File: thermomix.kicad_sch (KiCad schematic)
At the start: 30 parts, among them J101 DX07S016JA1R1500, J102 Conn_01x05, SW101 SW_Push, SW102 SW_Push, U101 MIC5353-3.3YMT, U102 TPD2E2U06, U103 STM32F303RDTx, Y101 Crystal_GND24

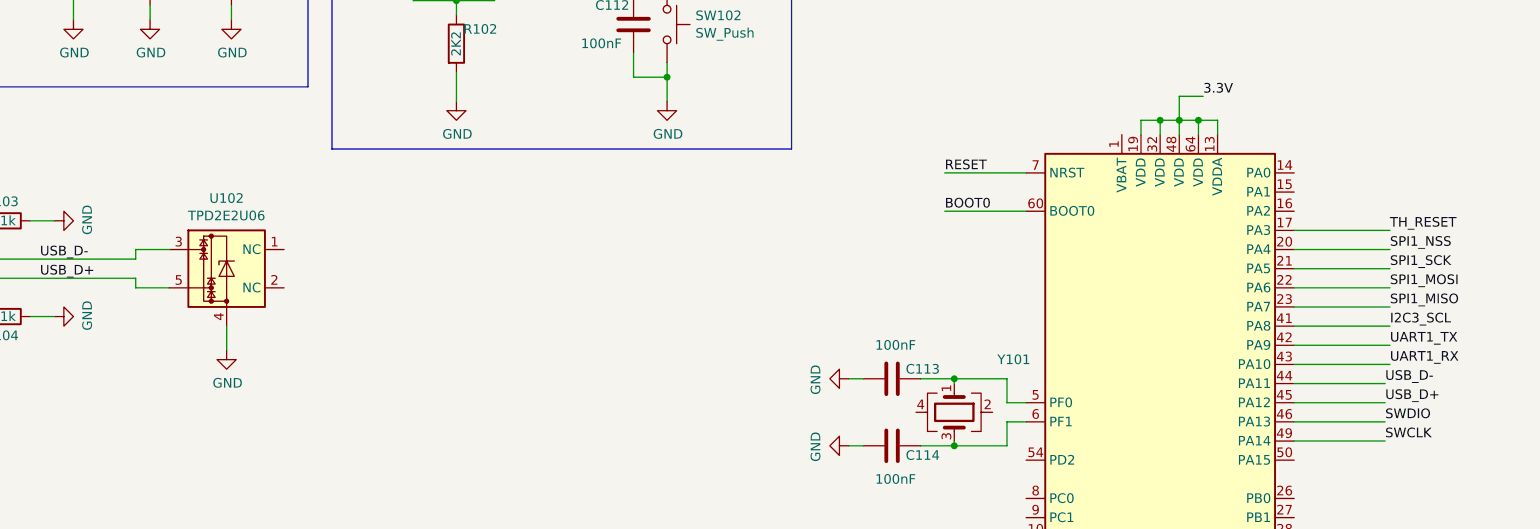
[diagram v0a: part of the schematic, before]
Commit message: Fixes issues from revision 1.0
Signed-off-by: Alexis Jeandet <alexis.jeandet@member.fsf.org>
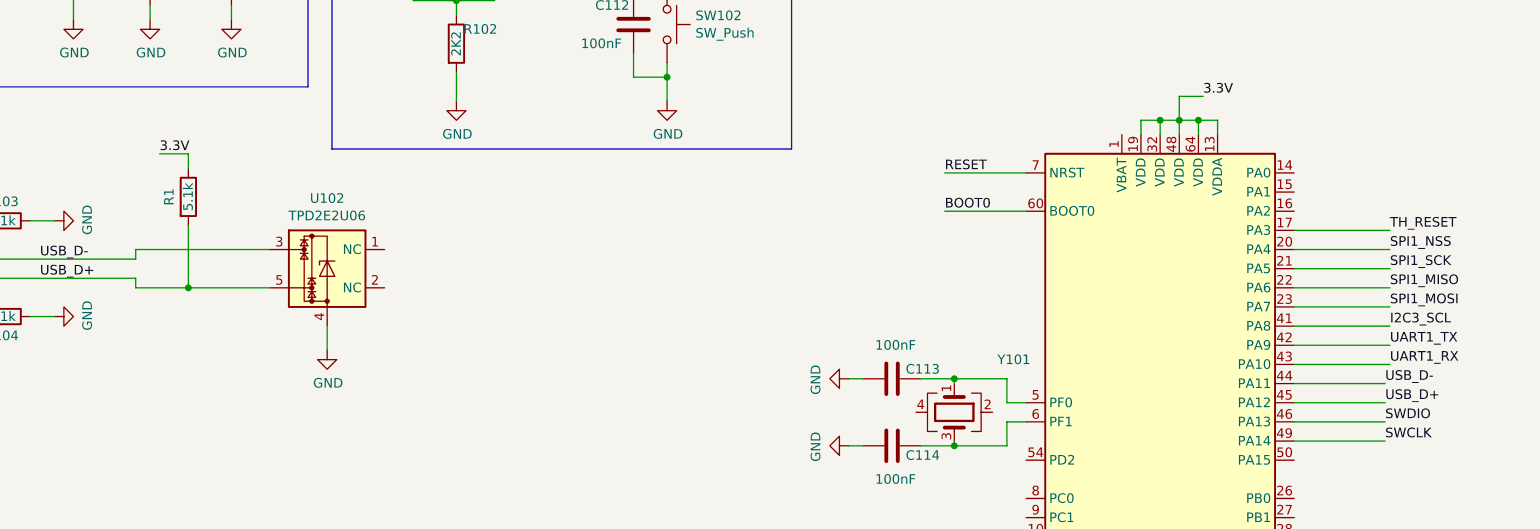
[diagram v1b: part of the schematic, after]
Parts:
- added R1: 5.1k, Resistor_SMD:R_0603_1608Metric_Pad0.98x0.95mm_HandSolder, symbol Device:R
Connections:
- net 3.3V: now also R1.1
- net SPI1_MISO: now also U103.22 (PA6); no longer U103.23 (PA7)
- net SPI1_MOSI: now also U103.23 (PA7); no longer U103.22 (PA6)
- net USB_D+: now also R1.2
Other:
- company: (none) -> LPP/CNRS
- moved on the sheet: U102
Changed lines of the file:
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@@
 (kicad_sch (version 20211123) (generator eeschema)
   (paper "A4")
+  (title_block
+    (date "2023-02-07")
+    (rev "1.1")
+    (company "LPP/CNRS")
+  )
   (junction (at 132.715 29.845) (diameter 0) (color 0 0 0 0)
   )
@@
   )
   (junction (at 198.755 91.44) (diameter 0) (color 0 0 0 0)
+  )
+  (junction (at 97.155 79.375) (diameter 0) (color 0 0 0 0)
   )
   (no_connect (at 65.405 73.025))
@@
     (stroke (width 0) (type default) (color 0 0 0 0))
   )
-  (wire (pts (xy 102.235 84.455) (xy 102.235 87.63))
+  (wire (pts (xy 93.345 61.595) (xy 97.155 61.595))
+    (stroke (width 0) (type default) (color 0 0 0 0))
+  )
+  (wire (pts (xy 115.57 84.455) (xy 115.57 87.63))
     (stroke (width 0) (type default) (color 0 0 0 0))
   )
@@
     (stroke (width 0) (type default) (color 0 0 0 0))
   )
+  (wire (pts (xy 97.155 61.595) (xy 97.155 63.5))
+    (stroke (width 0) (type default) (color 0 0 0 0))
+  )
   (wire (pts (xy 223.52 57.15) (xy 226.06 57.15))
     (stroke (width 0) (type default) (color 0 0 0 0))
@@
     (stroke (width 0) (type default) (color 0 0 0 0))
   )
-  (wire (pts (xy 94.615 79.375) (xy 90.17 79.375))
+  (wire (pts (xy 107.95 79.375) (xy 97.155 79.375))
     (stroke (width 0) (type default) (color 0 0 0 0))
   )
@@
     (stroke (width 0) (type default) (color 0 0 0 0))
   )
+  (wire (pts (xy 97.155 71.12) (xy 97.155 79.375))
+    (stroke (width 0) (type default) (color 0 0 0 0))
+  )
   (wire (pts (xy 233.68 57.15) (xy 233.68 59.055))
     (stroke (width 0) (type default) (color 0 0 0 0))
@@
     (stroke (width 0) (type default) (color 0 0 0 0))
   )
+  (wire (pts (xy 97.155 79.375) (xy 90.17 79.375))
+    (stroke (width 0) (type default) (color 0 0 0 0))
+  )
   (wire (pts (xy 102.87 43.815) (xy 102.87 41.91))
     (stroke (width 0) (type default) (color 0 0 0 0))
@@
     (stroke (width 0) (type default) (color 0 0 0 0))
   )
-  (wire (pts (xy 94.615 74.295) (xy 90.17 74.295))
+  (wire (pts (xy 107.95 74.295) (xy 90.17 74.295))
     (stroke (width 0) (type default) (color 0 0 0 0))
   )
@@
     (effects (font (size 1.27 1.27)) (justify left bottom))
   )
-  (label "SPI1_MISO" (at 256.54 81.915 0)
+  (label "SPI1_MISO" (at 256.54 79.375 0)
     (effects (font (size 1.27 1.27)) (justify left bottom))
   )
@@
     (effects (font (size 1.27 1.27)) (justify left bottom))
   )
-  (label "SPI1_MOSI" (at 256.54 79.375 0)
+  (label "SPI1_MOSI" (at 256.54 81.915 0)
     (effects (font (size 1.27 1.27)) (justify left bottom))
   )
@@
   )
   (label "RESET" (at 124.46 183.515 0)
+    (effects (font (size 1.27 1.27)) (justify left bottom))
+  )
+  (label "3.3V" (at 93.345 61.595 0)
     (effects (font (size 1.27 1.27)) (justify left bottom))
   )
@@
     )
     (pin "1")
+  )
+  (symbol (lib_id "Device:R") (at 97.155 67.31 0) (unit 1)
+    (in_bom yes) (on_board yes)
+    (property "Reference" "R1" (id 0) (at 94.615 67.31 90))
+    (property "Value" "5.1k" (id 1) (at 97.155 67.31 90))
+    (property "Footprint" "Resistor_SMD:R_0603_1608Metric_Pad0.98x0.95mm_HandSolder" (id 2) (at 95.377 67.31 90)
+      (effects (font (size 1.27 1.27)) hide)
+    )
+    (property "Datasheet" "~" (id 3) (at 97.155 67.31 0)
+      (effects (font (size 1.27 1.27)) hide)
+    )
+    (pin "1")
+    (pin "2")
   )
   (symbol (lib_id "power:GND") (at 240.03 33.02 0) (unit 1)
@@
     (pin "S6")
   )
-  (symbol (lib_id "Power_Protection:TPD2E2U06") (at 102.235 76.835 0) (unit 1)
-    (in_bom yes) (on_board yes)
-    (property "Reference" "U102" (id 0) (at 102.235 67.5132 0))
-    (property "Value" "TPD2E2U06" (id 1) (at 102.235 69.8246 0))
-    (property "Footprint" "Package_TO_SOT_SMD:SOT-553" (id 2) (at 81.915 83.185 0)
-      (effects (font (size 1.27 1.27)) hide)
-    )
-    (property "Datasheet" "http://www.ti.com/lit/ds/symlink/tpd2e2u06.pdf" (id 3) (at 97.155 71.755 0)
+  (symbol (lib_id "Power_Protection:TPD2E2U06") (at 115.57 76.835 0) (unit 1)
+    (in_bom yes) (on_board yes)
+    (property "Reference" "U102" (id 0) (at 115.57 67.5132 0))
+    (property "Value" "TPD2E2U06" (id 1) (at 115.57 69.8246 0))
+    (property "Footprint" "Package_TO_SOT_SMD:SOT-553" (id 2) (at 95.25 83.185 0)
+      (effects (font (size 1.27 1.27)) hide)
+    )
+    (property "Datasheet" "http://www.ti.com/lit/ds/symlink/tpd2e2u06.pdf" (id 3) (at 110.49 71.755 0)
       (effects (font (size 1.27 1.27)) hide)
     )
@@
     (pin "5")
   )
-  (symbol (lib_id "power:GND") (at 102.235 87.63 0) (unit 1)
-    (in_bom yes) (on_board yes)
-    (property "Reference" "#PWR0116" (id 0) (at 102.235 93.98 0)
-      (effects (font (size 1.27 1.27)) hide)
-    )
-    (property "Value" "GND" (id 1) (at 102.362 92.0242 0))
-    (property "Footprint" "" (id 2) (at 102.235 87.63 0)
-      (effects (font (size 1.27 1.27)) hide)
-    )
-    (property "Datasheet" "" (id 3) (at 102.235 87.63 0)
+  (symbol (lib_id "power:GND") (at 115.57 87.63 0) (unit 1)
+    (in_bom yes) (on_board yes)
+    (property "Reference" "#PWR0116" (id 0) (at 115.57 93.98 0)
+      (effects (font (size 1.27 1.27)) hide)
+    )
+    (property "Value" "GND" (id 1) (at 115.697 92.0242 0))
+    (property "Footprint" "" (id 2) (at 115.57 87.63 0)
+      (effects (font (size 1.27 1.27)) hide)
+    )
+    (property "Datasheet" "" (id 3) (at 115.57 87.63 0)
       (effects (font (size 1.27 1.27)) hide)
     )
@@
       (reference "#PWR0121") (unit 1) (value "GND") (footprint "")
     )
+    (path "/2d00094a-2185-46c6-a905-ea05001884a3/18c7fd1b-c790-4343-ba73-bdb31469d0c1"
+      (reference "#PWR0122") (unit 1) (value "GND") (footprint "")
+    )
     (path "/2d00094a-2185-46c6-a905-ea05001884a3/00000000-0000-0000-0000-00005cd1cca1"
       (reference "#PWR0201") (unit 1) (value "GND") (footprint "")
@@
       (reference "#PWR0232") (unit 1) (value "GND") (footprint "")
     )
-    (path "/2d00094a-2185-46c6-a905-ea05001884a3/18c7fd1b-c790-4343-ba73-bdb31469d0c1"
-      (reference "#PWR?") (unit 1) (value "GND") (footprint "")
-    )
     (path "/0e5c956a-0664-4fcf-9bb1-1eae993c2225"
       (reference "C101") (unit 1) (value "100nF") (footprint "Capacitor_SMD:C_0603_1608Metric_Pad1.08x0.95mm_HandSolder")
@@
       (reference "LOGO101") (unit 1) (value "Logo_Open_Hardware_Small") (footprint "Symbol:KiCad-Logo2_5mm_SilkScreen")
     )
+    (path "/123306b8-cb9d-4e79-b3ef-9159b90353fd"
+      (reference "R1") (unit 1) (value "5.1k") (footprint "Resistor_SMD:R_0603_1608Metric_Pad0.98x0.95mm_HandSolder")
+    )
     (path "/8a3d03e2-f2c7-455f-8484-ae69e20feae4"
